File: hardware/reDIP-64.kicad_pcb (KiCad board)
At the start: 6 copper layers, 25.4 x 50.8 mm, 149 parts, among them J1 USB4080, J2 Conn_01x20, J3 Conn_01x20, J4 Conn_01x20, J5 Conn_02x20_Odd_Even, J6 Conn_02x05_Odd_Even, Q1 PDTA143ZMB, SW1 KXT311LHS, U1 PTN5110NHQ, U10 FPF2495C, U11 TPS22916CN, U12 FAN53611, U13 NCP163AMX120TBG, U14 NCP115AMX250TCG, U15 NCP163AMX330TBG, U16 NCP163AMX120TBG, U17 SN74CBT16211ADGVR, U18 SN74CBT16211ADGVR, U19 SN74CBT16211ADGVR, U2 LFE5UM5G-25F-8MG285C, U20 SN74CBT16211ADGVR, U21 W957A8MFYA5I, U22 W25Q128JVPIM, U23 SGTL5000XNLA3, U3 FUSB340, U4 DSC1103CE2-135.0000, U5 FSUSB42UMX, U6 FPF2286, U7 FPF1048, U8 TPS22916CN, U9 FAN53610

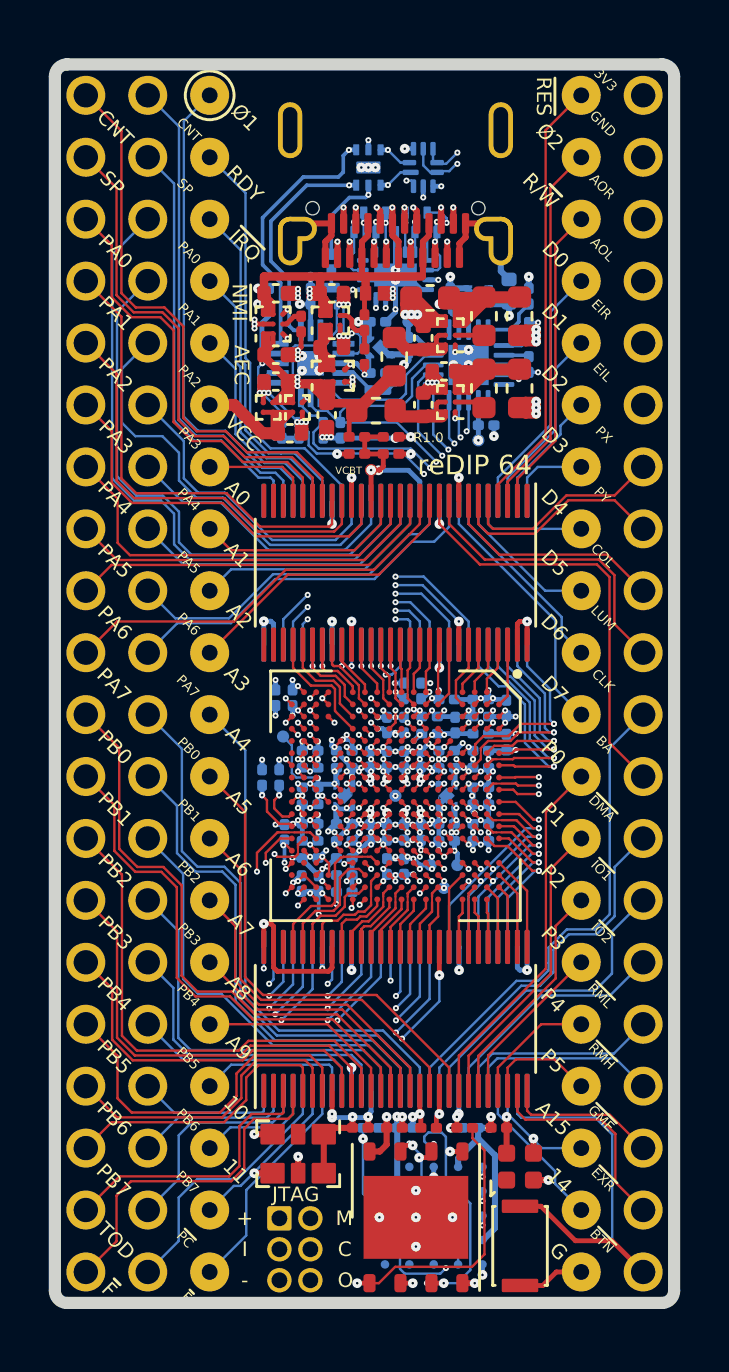
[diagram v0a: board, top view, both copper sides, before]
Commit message: Replaced socket pin headers with socket adapter
The socket adapter should hopefully *just* fit.
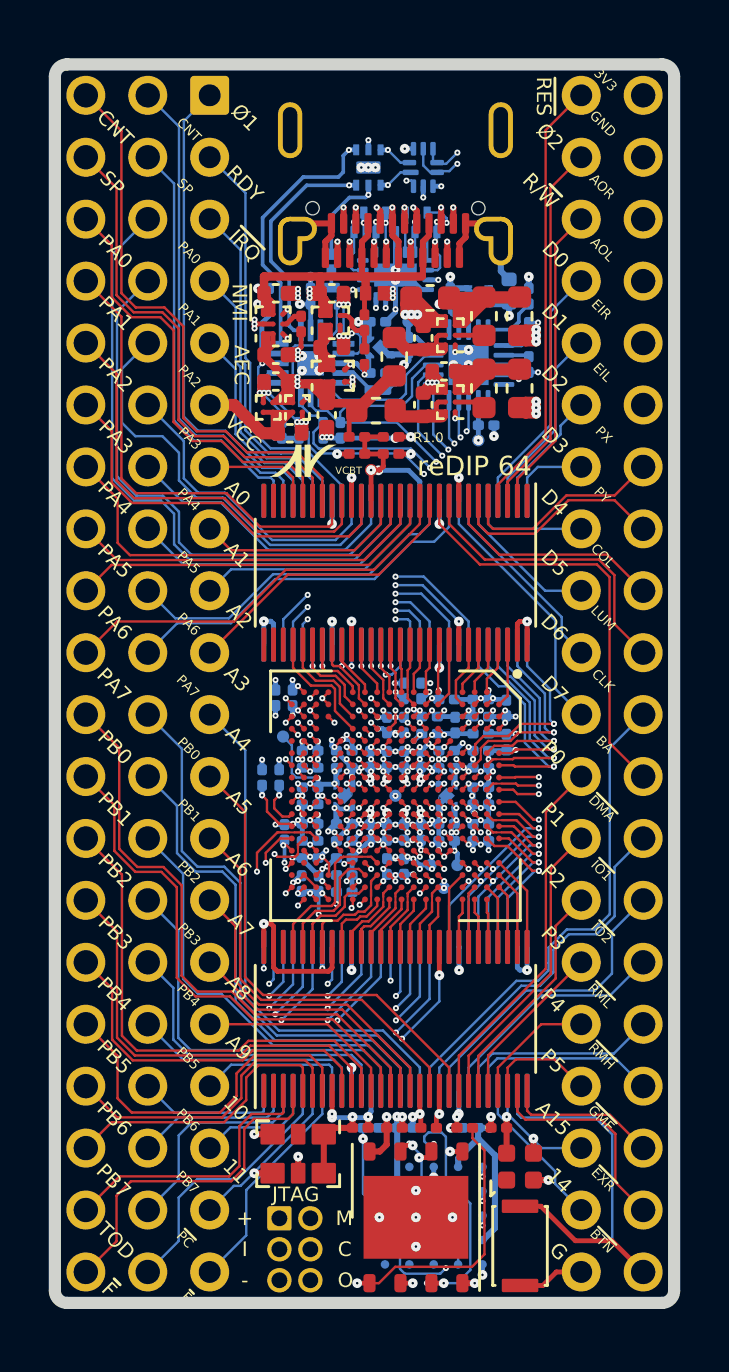
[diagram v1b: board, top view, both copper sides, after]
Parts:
- removed the J3 at (115.2, 100.0)
- removed MOS logo: G***, reDIP:MOS-logo
- removed the svg2mod at (107.5, 114.4)
- added svg2mod: G***, reDIP:Nimrod-N-small, F.Cu at (103.8, 115.0)
- added svg2mod: G***, reDIP:Nimrod-N-small, B.Cu at (111.5, 103.5)
- added svg2mod: G***, reDIP:MOS-logo-small, B.Cu at (108.2, 114.8)
- J2: value Conn_01x20 -> Conn_02x20_Counter_Clockwise; footprint reDIP:PinHeader_1x20_P2.54mm_Vertical_Machined -> reDIP:DIP-40_W15.24mm_Header
- renumbered J4 to J3, J5 to J4, J6 to J5
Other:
- board text removed: "pinout"

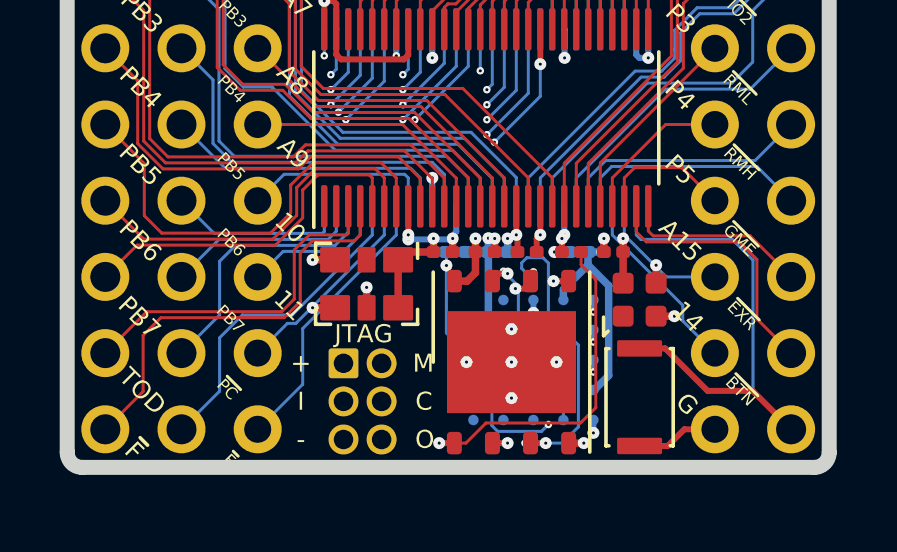
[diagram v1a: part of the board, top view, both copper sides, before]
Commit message: A few improvements
* Changed MCLK pullup to 4.7k
* A few pin swaps for cleaner routing
* Example pin headers in BOM
* Replaced reduced lifetime "mobile only" capacitors
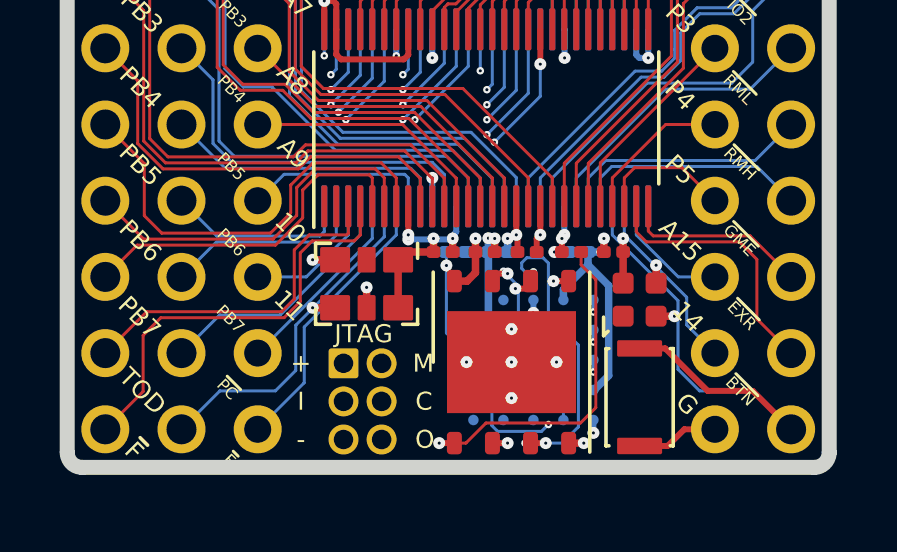
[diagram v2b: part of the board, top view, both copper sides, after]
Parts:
- R22: value 1k -> 4.7k
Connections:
- U2 pad A13: /FPGA_IO/I_A15 -> /FPGA_IO/I_A14
- U2 pad B12: /FPGA_IO/I_A14 -> /FPGA_IO/I_~{BTN}
- U2 pad B13: /FPGA_IO/I_~{BTN} -> /FPGA_IO/I_A15
- U2 pad C11: /FPGA_IO/I2_PB3 -> /FPGA_IO/I_~{IO1}
- U2 pad C12: /FPGA_IO/I_~{IO1} -> /FPGA_IO/I2_PB3
- U2 pad G15: /FPGA_IO/I_A12 -> /FPGA_IO/I2_~{FLAG}
- U2 pad H15: /FPGA_IO/I2_~{PC} -> /FPGA_IO/I_A11
- U2 pad H16: /FPGA_IO/I2_~{FLAG} -> /FPGA_IO/I_A12
- U2 pad J16: /FPGA_IO/I_A11 -> /FPGA_IO/I2_~{PC}
- U20 pad 2: /FPGA_IO/~{BTN} -> /FPGA_IO/A15
- U20 pad 23: /FPGA_IO/A12 -> /FPGA_IO/CIA2_~{FLAG}
- U20 pad 24: /FPGA_IO/CIA2_~{FLAG} -> /FPGA_IO/A12
- U20 pad 25: /FPGA_IO/A11 -> /FPGA_IO/CIA2_~{PC}
- U20 pad 26: /FPGA_IO/CIA2_~{PC} -> /FPGA_IO/A11
- U20 pad 3: /FPGA_IO/A15 -> /FPGA_IO/A14
- U20 pad 31: /FPGA_IO/I2_~{PC} -> /FPGA_IO/I_A11
- U20 pad 32: /FPGA_IO/I_A11 -> /FPGA_IO/I2_~{PC}
- U20 pad 33: /FPGA_IO/I2_~{FLAG} -> /FPGA_IO/I_A12
- U20 pad 34: /FPGA_IO/I_A12 -> /FPGA_IO/I2_~{FLAG}
- U20 pad 4: /FPGA_IO/A14 -> /FPGA_IO/~{BTN}
- U20 pad 52: /FPGA_IO/I_A14 -> /FPGA_IO/I_~{BTN}
- U20 pad 53: /FPGA_IO/I_A15 -> /FPGA_IO/I_A14
- U20 pad 54: /FPGA_IO/I_~{BTN} -> /FPGA_IO/I_A15
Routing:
- net /FPGA_IO/I_A12: track 15.7 -> 13.3 mm
- net /FPGA_IO/I2_~{FLAG}: track 13.3 -> 15.7 mm
- net /FPGA_IO/I_~{BTN}: track 6.92 -> 7.95 mm
- net /FPGA_IO/I_A15: track 7.56 -> 6.92 mm
- net /FPGA_IO/CIA2_~{PC}: track 9.14 -> 8.54 mm
- net /FPGA_IO/I2_PB3: track 16.0 -> 15.5 mm
- net /FPGA_IO/I_~{IO1}: track 17.2 -> 17.7 mm

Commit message: BOM correction, silk screen update
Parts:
- added svg2mod: G***, reDIP:Nimrod-text-small, B.Cu at (103.8, 103.9)
- moved svg2mod 0.21 mm to (111.3, 103.5)
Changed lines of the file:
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@@
     (descr "Resistor SMD 0201 (0603 Metric), square (rectangular) end terminal, IPC_7351 nominal, (Body size source: https://www.vishay.com/docs/20052/crcw0201e3.pdf), generated with kicad-footprint-generator")
     (tags "resistor")
-    (property "Description" "RES 1kΩ 50mW 1% 0201")
+    (property "Description" "RES 4.7kΩ 50mW 5% 0201")
     (property "Mfg" "Panasonic")
-    (property "PN" "ERJ1GNF1001C")
+    (property "PN" "ERJ1GNJ472C")
     (property "Sheetfile" "reDIP-64-Config.kicad_sch")
     (property "Sheetname" "Config_Memory")
@@
     )
   )
+  (footprint "reDIP:Nimrod-text-small" (layer "B.Cu")
+    (at 103.75 103.91 180)
+    (descr "Imported from graphics/Nimrod-logo.svg")
+    (tags "svg2mod")
+    (attr board_only exclude_from_pos_files exclude_from_bom)
+    (fp_text reference "svg2mod" (at 0 4.162601) (layer "B.SilkS") hide
+      (effects (font (size 1.524 1.524) (thickness 0.3048)) (justify mirror))
+    )
+    (fp_text value "G***" (at 0 -4.162601) (layer "B.SilkS") hide
+      (effects (font (size 1.524 1.524) (thickness 0.3048)) (justify mirror))
+    )
+    (fp_poly (pts
+        (xy 0.220811 0.169567)
+        (xy -0.0802 0.27449)
+        (xy -0.0802 -0.273941)
+        (xy 0.031793 -0.273941)
+        (xy 0.031793 -0.058885)
+        (xy 0.150115 -0.058885)
+        (xy 0.192667 -0.063259)
+        (xy 0.219139 -0.076372)
+        (xy 0.233134 -0.102604)
+        (xy 0.238295 -0.146321)
+        (xy 0.239035 -0.197294)
+        (xy 0.243872 -0.244547)
+        (xy 0.251323 -0.273941)
+        (xy 0.377455 -0.273941)
+        (xy 0.377455 -0.260174)
+        (xy 0.356617 -0.22892)
+        (xy 0.353642 -0.177947)
+        (xy 0.353642 -0.141112)
+        (xy 0.349684 -0.090841)
+        (xy 0.33782 -0.05535)
+        (xy 0.316475 -0.030472)
+        (xy 0.284057 -0.012004)
+        (xy 0.32303 0.009155)
+        (xy 0.349176 0.041388)
+        (xy 0.36396 0.079478)
+        (xy 0.368893 0.118221)
+        (xy 0.366286 0.148822)
+        (xy 0.358479 0.175892)
+        (xy 0.3302 0.222029)
+        (xy 0.306244 0.244255)
+        (xy 0.277548 0.260352)
+        (xy 0.239821 0.270395)
+        (xy 0.188807 0.27449)
+        (xy -0.0802 0.27449)
+        (xy 0.220811 0.169567)
+        (xy 0.245644 0.14426)
+        (xy 0.253926 0.102593)
+        (xy 0.245365 0.064082)
+        (xy 0.219689 0.040831)
+        (xy 0.195503 0.034133)
+        (xy 0.16165 0.0319)
+        (xy 0.031793 0.0319)
+        (xy 0.031793 0.17924)
+        (xy 0.164995 0.17924)
+        (xy 0.197554 0.176819)
+        (xy 0.220811 0.169567)
+      ) (layer "B.SilkS") (width 0) (fill solid))
+    (fp_poly (pts
+        (xy -0.463412 -0.156739)
+        (xy -0.364447 0.27449)
+        (xy -0.199622 0.27449)
+        (xy -0.199622 -0.273941)
+        (xy -0.306398 -0.273941)
+        (xy -0.306398 0.097013)
+        (xy -0.306028 0.141847)
+        (xy -0.305657 0.18631)
+        (xy -0.409469 -0.273941)
+        (xy -0.52071 -0.273941)
+        (xy -0.623782 0.18631)
+        (xy -0.623411 0.141847)
+        (xy -0.62303 0.097013)
+        (xy -0.62303 -0.273941)
+        (xy -0.729816 -0.273941)
+        (xy -0.729816 0.27449)
+        (xy -0.563128 0.27449)
+        (xy -0.463412 -0.156739)
+      ) (layer "B.SilkS") (width 0) (fill solid))
+    (fp_poly (pts
+        (xy -1.512813 -0.273941)
+        (xy -1.512813 0.27449)
+        (xy -1.392629 0.27449)
+        (xy -1.174231 -0.10837)
+        (xy -1.174231 0.27449)
+        (xy -1.067445 0.27449)
+        (xy -1.067445 -0.273941)
+        (xy -1.182041 -0.273941)
+        (xy -1.406027 0.115616)
+        (xy -1.406027 -0.273941)
+        (xy -1.512813 -0.273941)
+      ) (layer "B.SilkS") (width 0) (fill solid))
+    (fp_poly (pts
+        (xy -0.959188 0.27449)
+        (xy -0.959188 -0.273941)
+        (xy -0.845333 -0.273941)
+        (xy -0.845333 0.27449)
+        (xy -0.959188 0.27449)
+      ) (layer "B.SilkS") (width 0) (fill solid))
+    (fp_poly (pts
+        (xy 0.601261 -0.141856)
+        (xy 0.450184 0.058288)
+        (xy 0.44685 0.001019)
+        (xy 0.450184 -0.055301)
+        (xy 0.460185 -0.106082)
+        (xy 0.476854 -0.151326)
+        (xy 0.50019 -0.191032)
+        (xy 0.530194 -0.2252)
+        (xy 0.56472 -0.253202)
+        (xy 0.606179 -0.2732)
+        (xy 0.654572 -0.285197)
+        (xy 0.709898 -0.289196)
+        (xy 0.765219 -0.285197)
+        (xy 0.813611 -0.2732)
+        (xy 0.855076 -0.253202)
+        (xy 0.889614 -0.2252)
+        (xy 0.919482 -0.191032)
+        (xy 0.942714 -0.151326)
+        (xy 0.95931 -0.106082)
+        (xy 0.969268 -0.055301)
+        (xy 0.972587 0.001019)
+        (xy 0.969268 0.058288)
+        (xy 0.95931 0.109543)
+        (xy 0.942714 0.154787)
+        (xy 0.919482 0.194018)
+        (xy 0.889614 0.227238)
+        (xy 0.855076 0.255234)
+        (xy 0.813611 0.275233)
+        (xy 0.765219 0.287234)
+        (xy 0.709898 0.291234)
+        (xy 0.654572 0.287234)
+        (xy 0.606179 0.275233)
+        (xy 0.56472 0.255234)
+        (xy 0.530194 0.227238)
+        (xy 0.50019 0.194018)
+        (xy 0.476854 0.154787)
+        (xy 0.460185 0.109543)
+        (xy 0.450184 0.058288)
+        (xy 0.601261 -0.141856)
+        (xy 0.578723 -0.103657)
+        (xy 0.565208 -0.056032)
+        (xy 0.560705 0.001019)
+        (xy 0.565208 0.05807)
+        (xy 0.578723 0.105695)
+        (xy 0.601261 0.143894)
+        (xy 0.631352 0.171799)
+        (xy 0.667565 0.188542)
+        (xy 0.709898 0.194123)
+        (xy 0.752173 0.18852)
+        (xy 0.7882 0.171713)
+        (xy 0.817986 0.143708)
+        (xy 0.840206 0.105443)
+        (xy 0.853544 0.057879)
+        (xy 0.857991 0.001019)
+        (xy 0.853544 -0.056032)
+        (xy 0.840206 -0.103657)
+        (xy 0.817986 -0.141856)
+        (xy 0.7882 -0.169762)
+        (xy 0.752173 -0.186505)
+        (xy 0.709898 -0.192086)
+        (xy 0.667565 -0.186505)
+        (xy 0.631352 -0.169762)
+        (xy 0.601261 -0.141856)
+      ) (layer "B.SilkS") (width 0) (fill solid))
+    (fp_poly (pts
+        (xy 1.379623 0.132864)
+        (xy 1.497612 -0.13312)
+        (xy 1.511331 -0.08889)
+        (xy 1.519563 -0.040474)
+        (xy 1.522307 0.012127)
+        (xy 1.519699 0.056399)
+        (xy 1.511893 0.102912)
+        (xy 1.496908 0.14886)
+        (xy 1.472819 0.191465)
+        (xy 1.446566 0.221686)
+        (xy 1.415435 0.244879)
+        (xy 1.379432 0.261046)
+        (xy 1.341284 0.269599)
+        (xy 1.294596 0.272953)
+        (xy 1.058333 0.272953)
+        (xy 1.058333 -0.275483)
+        (xy 1.294596 -0.275483)
+        (xy 1.341715 -0.271391)
+        (xy 1.383654 -0.259113)
+        (xy 1.420416 -0.23865)
+        (xy 1.452 -0.21)
+        (xy 1.478407 -0.173164)
+        (xy 1.497612 -0.13312)
+        (xy 1.379623 0.132864)
+        (xy 1.394192 0.098653)
+        (xy 1.402934 0.055803)
+        (xy 1.405848 0.004313)
+        (xy 1.401472 -0.052153)
+        (xy 1.388365 -0.100238)
+        (xy 1.361571 -0.144682)
+        (xy 1.323866 -0.171346)
+        (xy 1.27525 -0.180233)
+        (xy 1.169585 -0.180233)
+        (xy 1.169585 0.177703)
+        (xy 1.27525 0.177703)
+        (xy 1.321573 0.172719)
+        (xy 1.356364 0.157771)
+        (xy 1.379623 0.132864)
+      ) (layer "B.SilkS") (width 0) (fill solid))
+  )
   (footprint "reDIP:TestPoint_Pad_D0.5mm" (layer "B.Cu")
     (at 103.01 126.3 180)
@@
   )
   (footprint "reDIP:Nimrod-N-small" (layer "B.Cu")
-    (at 111.53 103.54 180)
+    (at 111.32 103.53 180)
     (descr "Imported from Nimrod-N.svg")
     (tags "svg2mod")

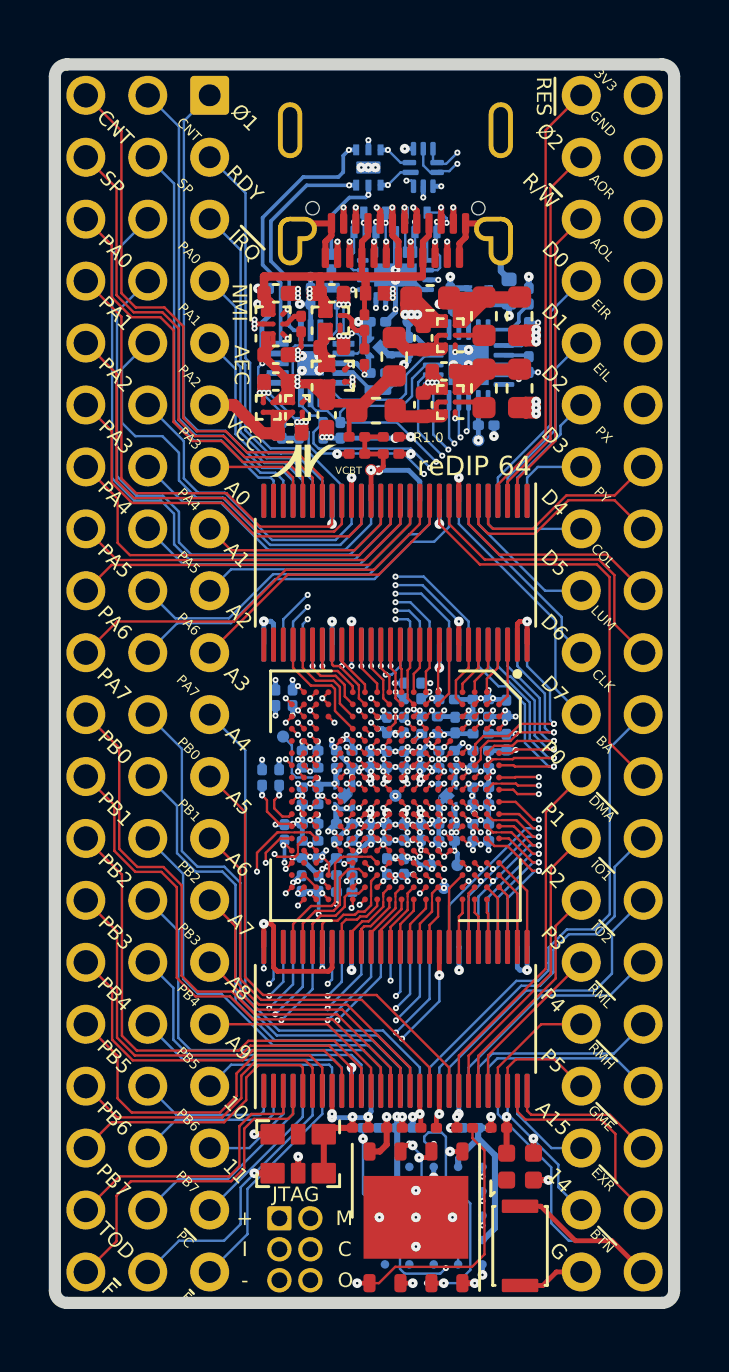
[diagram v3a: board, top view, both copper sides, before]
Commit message: Audio upgrade
* Changed from line out to headphone out with 10uF tantalum capacitors
* PTN5110 decoupling capacitor QA
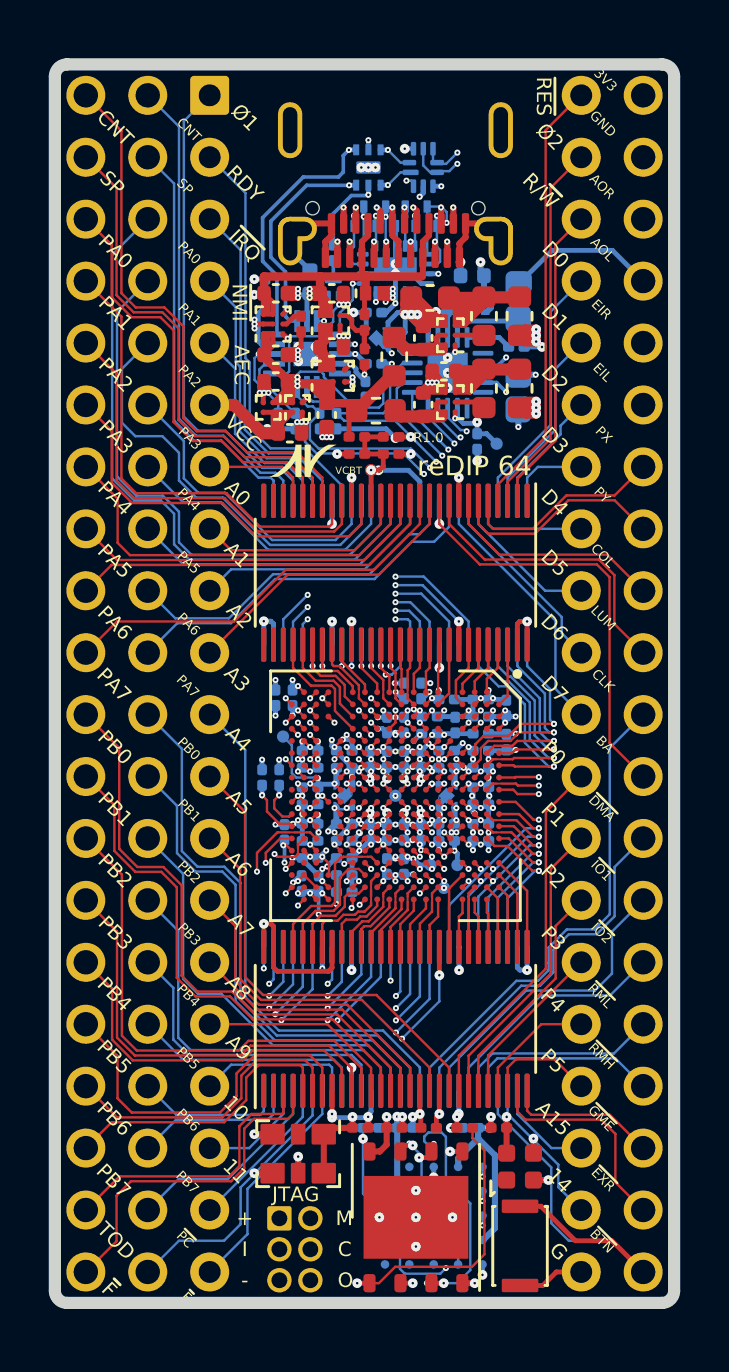
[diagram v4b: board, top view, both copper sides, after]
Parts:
- C1: footprint Capacitor_SMD:C_0201_0603Metric -> Capacitor_SMD:C_0402_1005Metric
- C69, C70: value 1uF -> 10uF; footprint Capacitor_SMD:C_0201_0603Metric -> Capacitor_Tantalum_SMD:CP_EIA-1608-08_AVX-J
- moved C70 2.62 mm to (112.7, 108.5)
- moved C69 2.57 mm to (112.7, 112.2), turned to 90 degrees
- moved C68 2.14 mm to (112.6, 110.3), turned to 0 degrees
- moved C27 1.64 mm to (110.8, 107.4), turned to 180 degrees
- moved C30 1.35 mm to (108.3, 108.9), turned to 0 degrees
- moved U23 0.92 mm to (109.8, 111.4)
- moved C67 0.77 mm to (111.0, 114.2), turned to -90 degrees
- moved TP5 0.76 mm to (111.8, 114.3)
- moved TP6 0.76 mm to (107.8, 110.0)
- moved C1 0.59 mm to (104.1, 107.7)
- moved C4 0.51 mm to (106.4, 112.1), turned to -90 degrees
- moved C29 0.41 mm to (106.7, 108.9)
- moved U16 0.41 mm to (106.8, 110.0)
- moved C2 0.41 mm to (106.7, 111.0)
- moved R1 0.41 mm to (105.2, 113.4)
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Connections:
- C69 pad 1: /Audio/AUDIO_OUT_R -> Net-(C69-Pad1)
- C69 pad 2: Net-(C69-Pad2) -> /Audio/AUDIO_OUT_R
- C70 pad 1: /Audio/AUDIO_OUT_L -> Net-(C70-Pad1)
- C70 pad 2: Net-(C70-Pad2) -> /Audio/AUDIO_OUT_L
- U23 pad 1: unconnected-(U23-Pad1) -> Net-(C69-Pad1)
- U23 pad 4: unconnected-(U23-Pad4) -> Net-(C70-Pad1)
- U23 pad 6: Net-(C69-Pad2) -> unconnected-(U23-Pad6)
- U23 pad 7: Net-(C70-Pad2) -> unconnected-(U23-Pad7)
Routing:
- net Net-(C69-Pad1): track 0.00 -> 10.2 mm, vias 0 -> 4
- net Net-(C70-Pad1): track 0.00 -> 3.07 mm
- net /Audio/AUDIO_OUT_R: track 7.36 -> 9.61 mm
- net /Audio/EXT_IN_R: track 6.41 -> 7.62 mm
- net /Power/EN_SNK: track 3.34 -> 2.15 mm
- net Net-(C69-Pad2): track 1.14 -> 0.00 mm
- net GND: track 167.2 -> 166.1 mm, vias 277 -> 279
- net Net-(C70-Pad2): track 1.04 -> 0.00 mm
- net /Audio/EXT_IN_L: track 6.40 -> 7.43 mm
- net VDDD: track 2.52 -> 3.40 mm
- net /Audio/I2C_SDA: track 28.0 -> 27.2 mm
- net VBUS: track 25.0 -> 25.7 mm
- net +5V: track 52.4 -> 51.8 mm
- net +3V3: track 80.6 -> 80.8 mm, vias 63 -> 65
- net /Audio/AUDIO_OUT_L: track 6.85 -> 6.70 mm, vias 2 -> 0
